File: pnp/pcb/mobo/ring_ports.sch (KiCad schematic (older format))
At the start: 65 parts, among them J10 F06, J11 F07, J12 F08, J13 F09, J14 F10, J15 F11, J16 F12, J17 F13, J18 F14, J19 F15, J20 F16, J21 F17, J22 F18, J23 F19, J24 F20, J25 F25, J26 F26, J27 F27, J28 F28, J29 F21, J30 F22, J31 F23, J32 F24, J33 F29, J34 F30, J35 F31, J36 F32, J47 I2C_1, J48 I2C_2, J49 I2C_3, J5 F01, J6 F02, J7 F03, J8 F04, J9 F05, U1 MCP23017_SO_2, U3 MCP23017_SO_3, U4 MCP23017_SO_1, U5 MCP23017_SO_4

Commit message: Removing KiCad cache and bak files. Removing fabrication outputs. Updated Marlin to use the correct stepper driver for the Z and Y axis.
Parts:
- J10, J11, J12, J13, J14, J15, J16, J17, J18, J19, J20, J21, J22, J23, J24, J25, J26, J27, J28, J29, J30, J31, J32, J33, J34, J35, J36, J5, J6, J7, J8, J9: footprint Connector_JST:JST_PH_B4B-PH-K_1x04_P2.00mm_Vertical -> Connector_JST:JST_PH_B4B-PH-SM4-TB_1x04-1MP_P2.00mm_Vertical
- J47, J48, J49: footprint Connector_PinHeader_2.54mm:PinHeader_1x04_P2.54mm_Horizontal -> Connector_PinHeader_2.54mm:PinHeader_1x04_P2.54mm_Vertical

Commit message: REV000 motherboard routing complete
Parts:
- removed J48: I2C_2, Connector_PinHeader_2.54mm:PinHeader_1x04_P2.54mm_Vertical, symbol Connector:Conn_01x04_Male
- removed J49: I2C_3, Connector_PinHeader_2.54mm:PinHeader_1x04_P2.54mm_Vertical, symbol Connector:Conn_01x04_Male
- J10, J11, J12, J13, J14, J15, J16, J17, J18, J19, J20, J21, J22, J23, J24, J25, J26, J27, J28, J29, J30, J31, J32, J33, J34, J35, J36, J5, J6, J7, J8, J9: footprint Connector_JST:JST_PH_B4B-PH-SM4-TB_1x04-1MP_P2.00mm_Vertical -> Connector_JST:JST_PH_B4B-PH-K_1x04_P2.00mm_Vertical

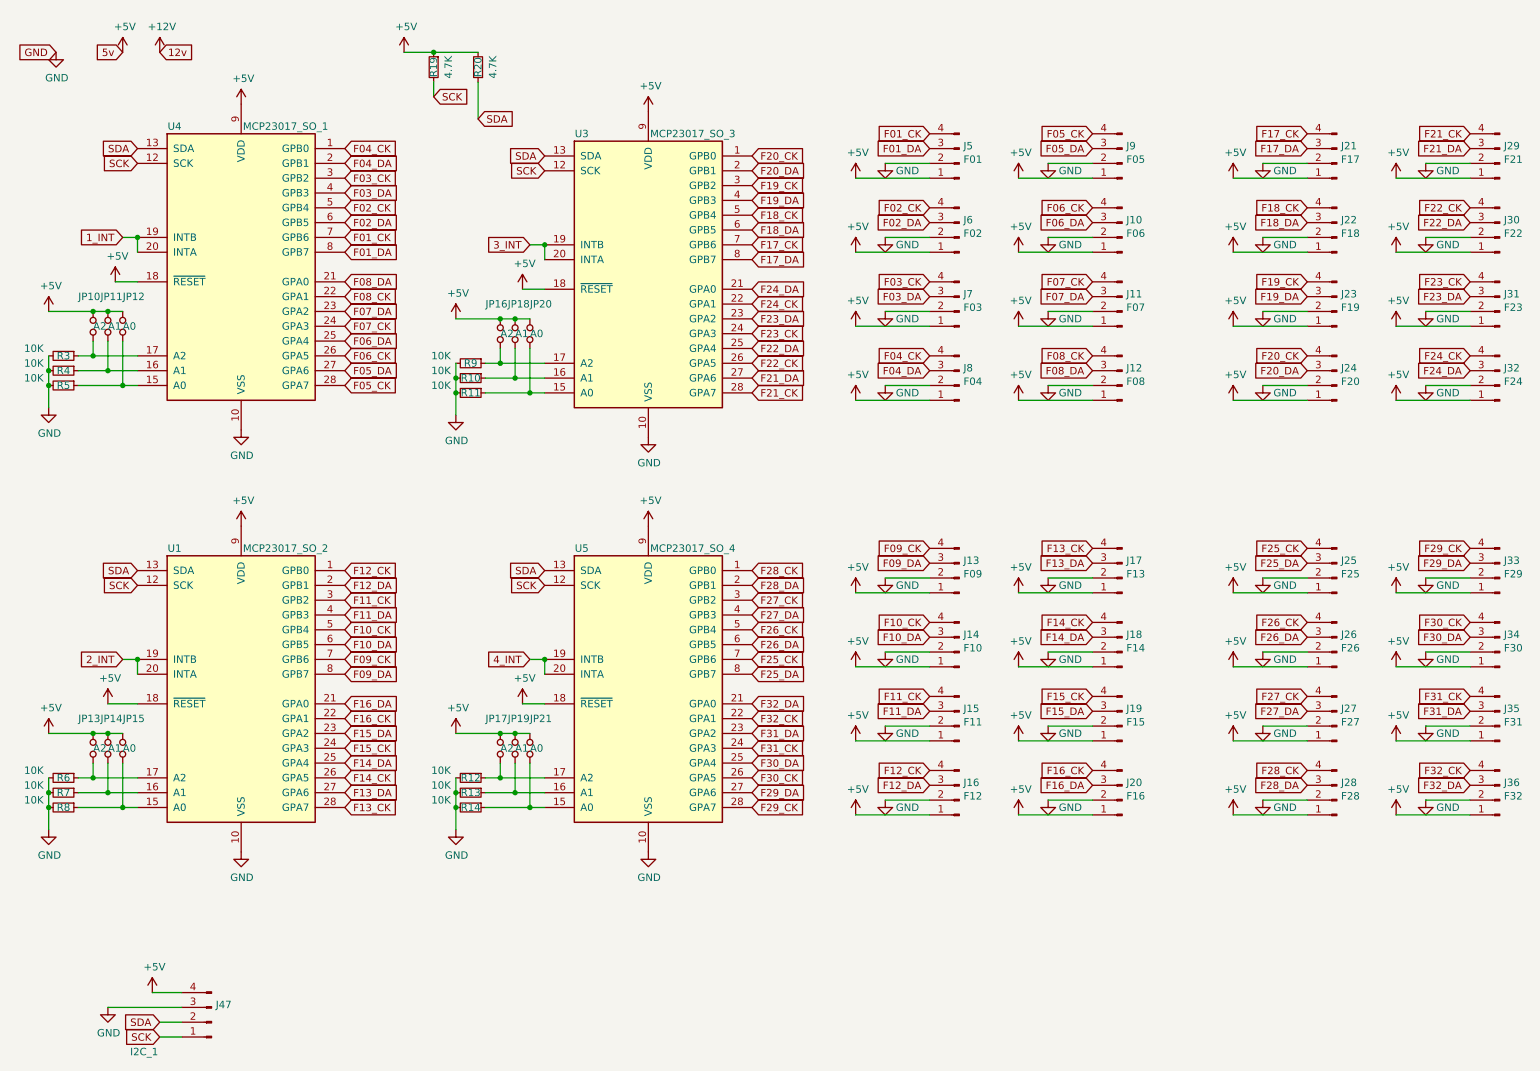
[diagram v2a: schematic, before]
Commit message: updating marlin pin assignments for REV000 mobo. changing mobo schematic to reflect these pin assignments (some pins in REV000 are unaccessible by marlin, all REV000 boards need to be patched to fit this pin assignment)
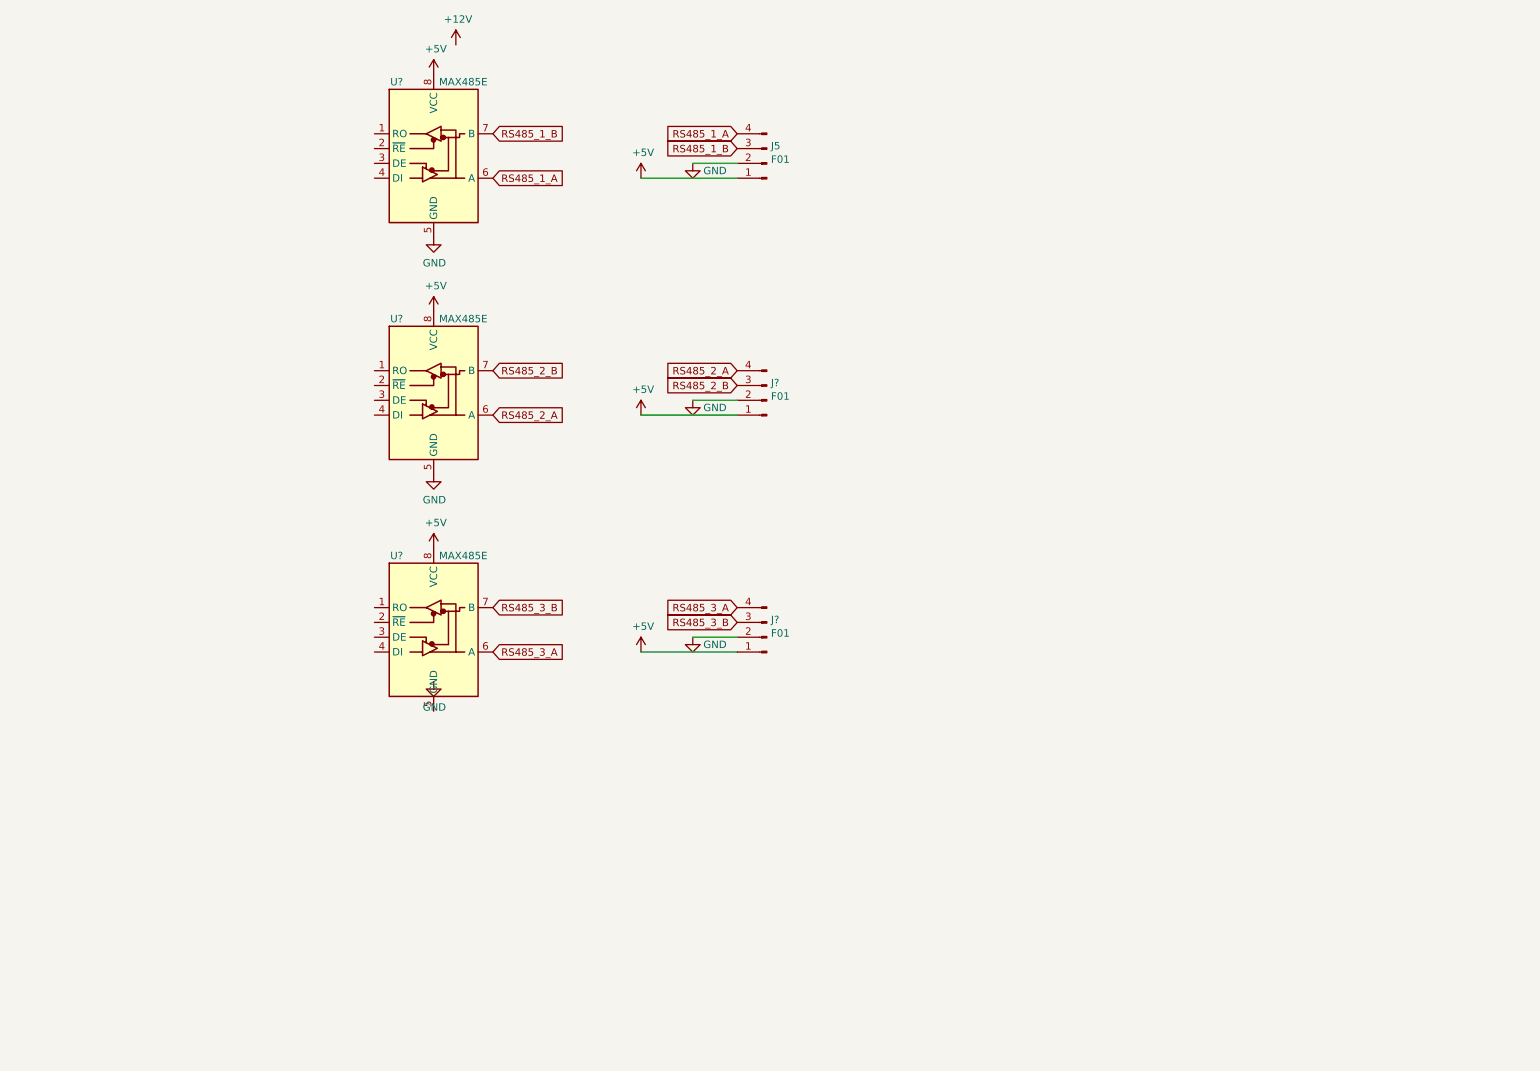
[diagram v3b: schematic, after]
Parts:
- removed J10: F06, Connector_JST:JST_PH_B4B-PH-K_1x04_P2.00mm_Vertical, symbol Connector:Conn_01x04_Male
- removed J11: F07, Connector_JST:JST_PH_B4B-PH-K_1x04_P2.00mm_Vertical, symbol Connector:Conn_01x04_Male
- removed J12: F08, Connector_JST:JST_PH_B4B-PH-K_1x04_P2.00mm_Vertical, symbol Connector:Conn_01x04_Male
- removed J13: F09, Connector_JST:JST_PH_B4B-PH-K_1x04_P2.00mm_Vertical, symbol Connector:Conn_01x04_Male
- removed J14: F10, Connector_JST:JST_PH_B4B-PH-K_1x04_P2.00mm_Vertical, symbol Connector:Conn_01x04_Male
- removed J15: F11, Connector_JST:JST_PH_B4B-PH-K_1x04_P2.00mm_Vertical, symbol Connector:Conn_01x04_Male
- removed J16: F12, Connector_JST:JST_PH_B4B-PH-K_1x04_P2.00mm_Vertical, symbol Connector:Conn_01x04_Male
- removed J17: F13, Connector_JST:JST_PH_B4B-PH-K_1x04_P2.00mm_Vertical, symbol Connector:Conn_01x04_Male
- removed J18: F14, Connector_JST:JST_PH_B4B-PH-K_1x04_P2.00mm_Vertical, symbol Connector:Conn_01x04_Male
- removed J19: F15, Connector_JST:JST_PH_B4B-PH-K_1x04_P2.00mm_Vertical, symbol Connector:Conn_01x04_Male
- removed J20: F16, Connector_JST:JST_PH_B4B-PH-K_1x04_P2.00mm_Vertical, symbol Connector:Conn_01x04_Male
- removed J21: F17, Connector_JST:JST_PH_B4B-PH-K_1x04_P2.00mm_Vertical, symbol Connector:Conn_01x04_Male
- removed J22: F18, Connector_JST:JST_PH_B4B-PH-K_1x04_P2.00mm_Vertical, symbol Connector:Conn_01x04_Male
- removed J23: F19, Connector_JST:JST_PH_B4B-PH-K_1x04_P2.00mm_Vertical, symbol Connector:Conn_01x04_Male
- removed J24: F20, Connector_JST:JST_PH_B4B-PH-K_1x04_P2.00mm_Vertical, symbol Connector:Conn_01x04_Male
- removed J25: F25, Connector_JST:JST_PH_B4B-PH-K_1x04_P2.00mm_Vertical, symbol Connector:Conn_01x04_Male
- removed J26: F26, Connector_JST:JST_PH_B4B-PH-K_1x04_P2.00mm_Vertical, symbol Connector:Conn_01x04_Male
- removed J27: F27, Connector_JST:JST_PH_B4B-PH-K_1x04_P2.00mm_Vertical, symbol Connector:Conn_01x04_Male
- removed J28: F28, Connector_JST:JST_PH_B4B-PH-K_1x04_P2.00mm_Vertical, symbol Connector:Conn_01x04_Male
- removed J29: F21, Connector_JST:JST_PH_B4B-PH-K_1x04_P2.00mm_Vertical, symbol Connector:Conn_01x04_Male
- removed J30: F22, Connector_JST:JST_PH_B4B-PH-K_1x04_P2.00mm_Vertical, symbol Connector:Conn_01x04_Male
- removed J31: F23, Connector_JST:JST_PH_B4B-PH-K_1x04_P2.00mm_Vertical, symbol Connector:Conn_01x04_Male
- removed J32: F24, Connector_JST:JST_PH_B4B-PH-K_1x04_P2.00mm_Vertical, symbol Connector:Conn_01x04_Male
- removed J33: F29, Connector_JST:JST_PH_B4B-PH-K_1x04_P2.00mm_Vertical, symbol Connector:Conn_01x04_Male
- removed J34: F30, Connector_JST:JST_PH_B4B-PH-K_1x04_P2.00mm_Vertical, symbol Connector:Conn_01x04_Male
- removed J35: F31, Connector_JST:JST_PH_B4B-PH-K_1x04_P2.00mm_Vertical, symbol Connector:Conn_01x04_Male
- removed J36: F32, Connector_JST:JST_PH_B4B-PH-K_1x04_P2.00mm_Vertical, symbol Connector:Conn_01x04_Male
- removed J47: I2C_1, Connector_PinHeader_2.54mm:PinHeader_1x04_P2.54mm_Vertical, symbol Connector:Conn_01x04_Male
- removed J6: F02, Connector_JST:JST_PH_B4B-PH-K_1x04_P2.00mm_Vertical, symbol Connector:Conn_01x04_Male
- removed J7: F03, Connector_JST:JST_PH_B4B-PH-K_1x04_P2.00mm_Vertical, symbol Connector:Conn_01x04_Male
- removed J8: F04, Connector_JST:JST_PH_B4B-PH-K_1x04_P2.00mm_Vertical, symbol Connector:Conn_01x04_Male
- removed J9: F05, Connector_JST:JST_PH_B4B-PH-K_1x04_P2.00mm_Vertical, symbol Connector:Conn_01x04_Male
- removed JP10, JP13, JP16, JP17: A2, Jumper:SolderJumper-2_P1.3mm_Open_RoundedPad1.0x1.5mm, symbol Device:Jumper_NO_Small
- removed JP11, JP14, JP18, JP19: A1, Jumper:SolderJumper-2_P1.3mm_Open_RoundedPad1.0x1.5mm, symbol Device:Jumper_NO_Small
- removed JP12, JP15, JP20, JP21: A0, Jumper:SolderJumper-2_P1.3mm_Open_RoundedPad1.0x1.5mm, symbol Device:Jumper_NO_Small
- removed R10, R11, R12, R13, R14, R3, R4, R5, R6, R7, R8, R9: 10K, Resistor_SMD:R_0805_2012Metric_Pad1.15x1.40mm_HandSolder, symbol Device:R_Small
- removed R19, R20: 4.7K, Resistor_SMD:R_0805_2012Metric_Pad1.15x1.40mm_HandSolder, symbol Device:R_Small
- removed U1: MCP23017_SO_2, Package_SO:SOIC-28W_7.5x17.9mm_P1.27mm, symbol Interface_Expansion:MCP23017_SO
- removed U3: MCP23017_SO_3, Package_SO:SOIC-28W_7.5x17.9mm_P1.27mm, symbol Interface_Expansion:MCP23017_SO
- removed U4: MCP23017_SO_1, Package_SO:SOIC-28W_7.5x17.9mm_P1.27mm, symbol Interface_Expansion:MCP23017_SO
- removed U5: MCP23017_SO_4, Package_SO:SOIC-28W_7.5x17.9mm_P1.27mm, symbol Interface_Expansion:MCP23017_SO
- added J? (x2): F01, Connector_JST:JST_PH_B4B-PH-K_1x04_P2.00mm_Vertical, symbol Connector:Conn_01x04_Male
- added U? (x3): MAX485E, symbol Interface_UART:MAX485E
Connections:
- net +5V: now also J?.1 (Pin_1), J?.1 (Pin_1), U?.8 (VCC), U?.8 (VCC), U?.8 (VCC)
- net GND: now also J?.2 (Pin_2), J?.2 (Pin_2), U?.5 (GND), U?.5 (GND)
- net F01_CK renamed RS485_1_A
- net RS485_1_A: now also U?.6 (A)
- net F01_DA renamed RS485_1_B
- net RS485_1_B: now also U?.7 (B)
- new net RS485_2_A: J?.4 (Pin_4), U?.6 (A)
- new net RS485_2_B: J?.3 (Pin_3), U?.7 (B)
- new net RS485_3_A: J?.4 (Pin_4), U?.6 (A)
- new net RS485_3_B: J?.3 (Pin_3), U?.7 (B)
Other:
- moved on the sheet: J5

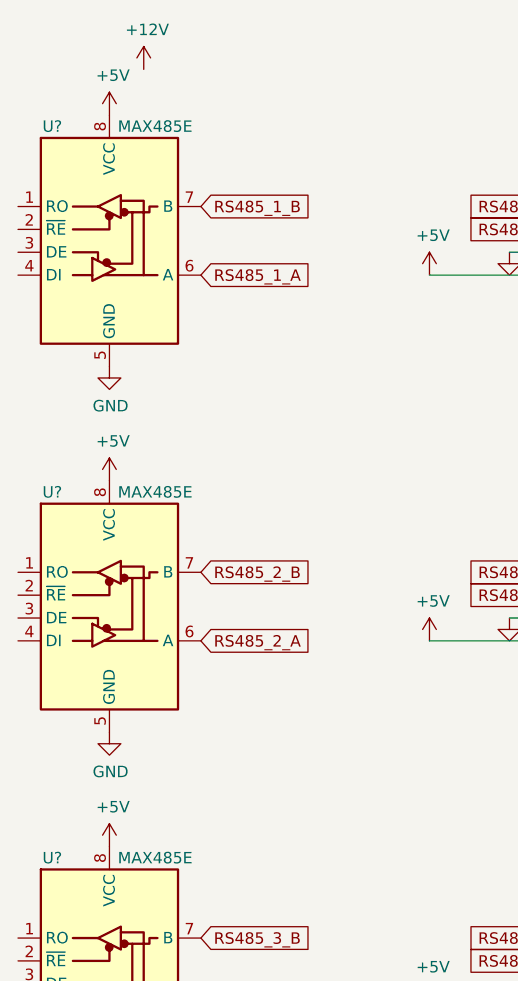
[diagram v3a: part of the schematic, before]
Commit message: updated buck converter passive values to match what works (5.238v output, no load), separated logic 5v and power 5v as separate nets with a NC jumper
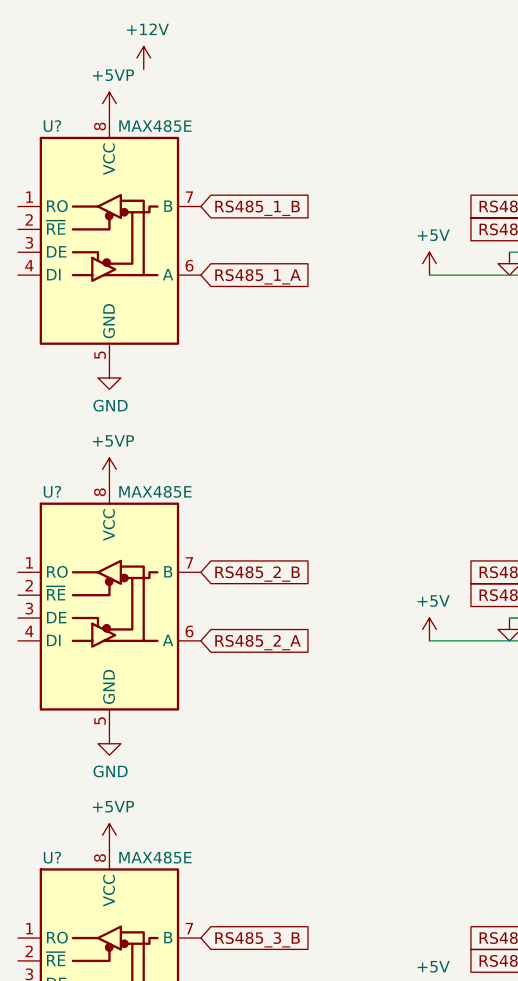
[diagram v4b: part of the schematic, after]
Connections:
- net +5V: no longer U?.8 (VCC), U?.8 (VCC), U?.8 (VCC)
- new net +5VP: U?.8 (VCC), U?.8 (VCC), U?.8 (VCC)
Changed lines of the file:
@@
-$EndComp
-$Comp
-L power:+5V #PWR?
-U 1 1 5EE729F9
-P 3400 900
-F 0 "#PWR?" H 3400 750 50  0001 C CNN
-F 1 "+5V" H 3415 1073 50  0000 C CNN
-F 2 "" H 3400 900 50  0001 C CNN
-F 3 "" H 3400 900 50  0001 C CNN
-	1    3400 900
-	1    0    0    -1
 $EndComp
 $Comp
@@
 $EndComp
 $Comp
-L power:+5V #PWR?
-U 1 1 5EE74122
+L power:+5VP #PWR?
+U 1 1 5EE7D6BC
+P 3400 4100
+AR Path="/5EE7D6BC" Ref="#PWR?"  Part="1"
+AR Path="/5EB0C364/5EE7D6BC" Ref="#PWR?"  Part="1"
+F 0 "#PWR?" H 3400 3950 50  0001 C CNN
+F 1 "+5VP" H 3415 4273 50  0000 C CNN
+F 2 "" H 3400 4100 50  0001 C CNN
+F 3 "" H 3400 4100 50  0001 C CNN
+	1    3400 4100
+	1    0    0    -1
+$EndComp
+$Comp
+L power:+5VP #PWR?
+U 1 1 5EE7D75B
 P 3400 2500
+AR Path="/5EE7D75B" Ref="#PWR?"  Part="1"
+AR Path="/5EB0C364/5EE7D75B" Ref="#PWR?"  Part="1"
 F 0 "#PWR?" H 3400 2350 50  0001 C CNN
-F 1 "+5V" H 3415 2673 50  0000 C CNN
+F 1 "+5VP" H 3415 2673 50  0000 C CNN
 F 2 "" H 3400 2500 50  0001 C CNN
 F 3 "" H 3400 2500 50  0001 C CNN
@@
 $EndComp
 $Comp
-L power:+5V #PWR?
-U 1 1 5EE7466D
-P 3400 4100
-F 0 "#PWR?" H 3400 3950 50  0001 C CNN
-F 1 "+5V" H 3415 4273 50  0000 C CNN
-F 2 "" H 3400 4100 50  0001 C CNN
-F 3 "" H 3400 4100 50  0001 C CNN
-	1    3400 4100
+L power:+5VP #PWR?
+U 1 1 5EE7DCA6
+P 3400 900
+AR Path="/5EE7DCA6" Ref="#PWR?"  Part="1"
+AR Path="/5EB0C364/5EE7DCA6" Ref="#PWR?"  Part="1"
+F 0 "#PWR?" H 3400 750 50  0001 C CNN
+F 1 "+5VP" H 3415 1073 50  0000 C CNN
+F 2 "" H 3400 900 50  0001 C CNN
+F 3 "" H 3400 900 50  0001 C CNN
+	1    3400 900
 	1    0    0    -1
 $EndComp

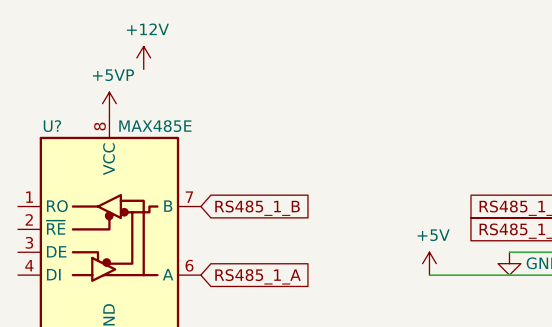
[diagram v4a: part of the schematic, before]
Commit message: Clean up Main PCB symbology
there is still an issue with the USB hub chip not working correctly, as it is reliant on a library outside the working folder structure
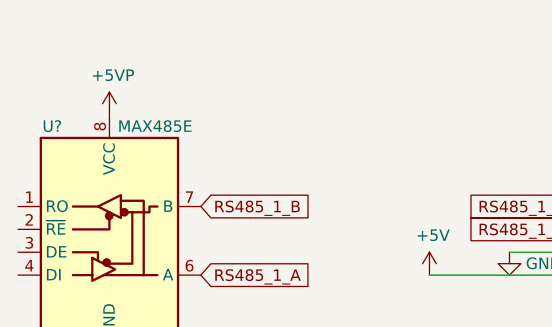
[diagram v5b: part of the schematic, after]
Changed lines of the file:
@@
 EESchema Schematic File Version 4
+LIBS:mobo-cache
 EELAYER 30 0
 EELAYER END
@@
 	1    0    0    -1
 $EndComp
-$Comp
-L power:+12V #PWR?
-U 1 1 5EE72E04
-P 3550 700
-F 0 "#PWR?" H 3550 550 50  0001 C CNN
-F 1 "+12V" H 3565 873 50  0000 C CNN
-F 2 "" H 3550 700 50  0001 C CNN
-F 3 "" H 3550 700 50  0001 C CNN
-	1    3550 700
-	1    0    0    -1
-$EndComp
